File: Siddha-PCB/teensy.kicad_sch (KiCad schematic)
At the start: 1 part, among them U1 Teensy LC

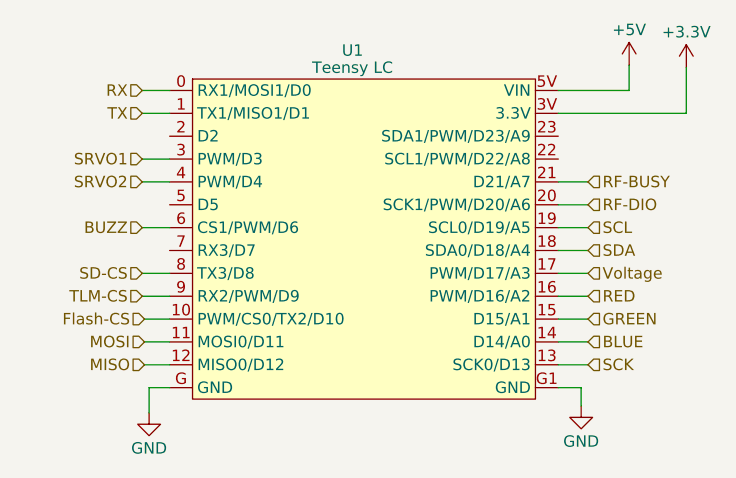
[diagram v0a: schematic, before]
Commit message: switch to linear actuator and 7.4v battery
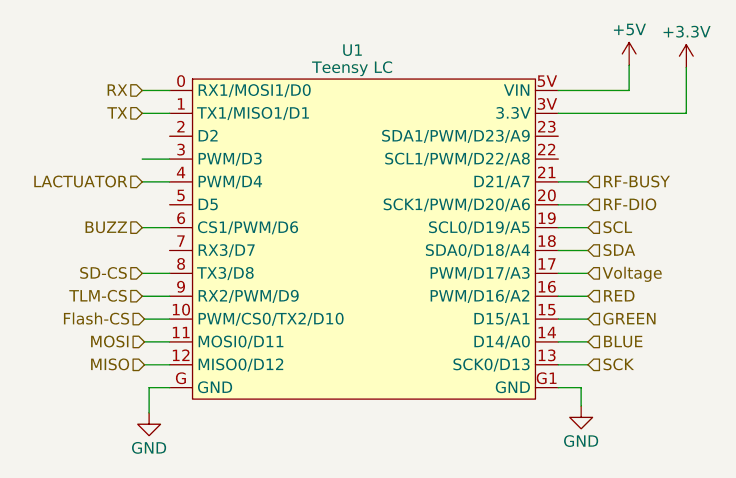
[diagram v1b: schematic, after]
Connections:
- net SRVO1: no longer names the net of U1.3 (PWM/D3)
- net SRVO2 renamed LACTUATOR
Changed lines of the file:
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@@
     (effects (font (size 1.27 1.27)) (justify left))
   )
-  (hierarchical_label "SRVO2" (shape input) (at 120.65 96.52 180) (fields_autoplaced)
+  (hierarchical_label "LACTUATOR" (shape input) (at 120.65 96.52 180) (fields_autoplaced)
     (effects (font (size 1.27 1.27)) (justify right))
   )
@@
     (effects (font (size 1.27 1.27)) (justify right))
   )
-  (hierarchical_label "SRVO1" (shape input) (at 120.65 93.98 180) (fields_autoplaced)
-    (effects (font (size 1.27 1.27)) (justify right))
-  )
